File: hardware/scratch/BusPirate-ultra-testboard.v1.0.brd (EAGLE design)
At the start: 40.3 x 44.4 mm, 20 parts, among them J1 CON_HEADER_1X10-RIGHT_ANGLED_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

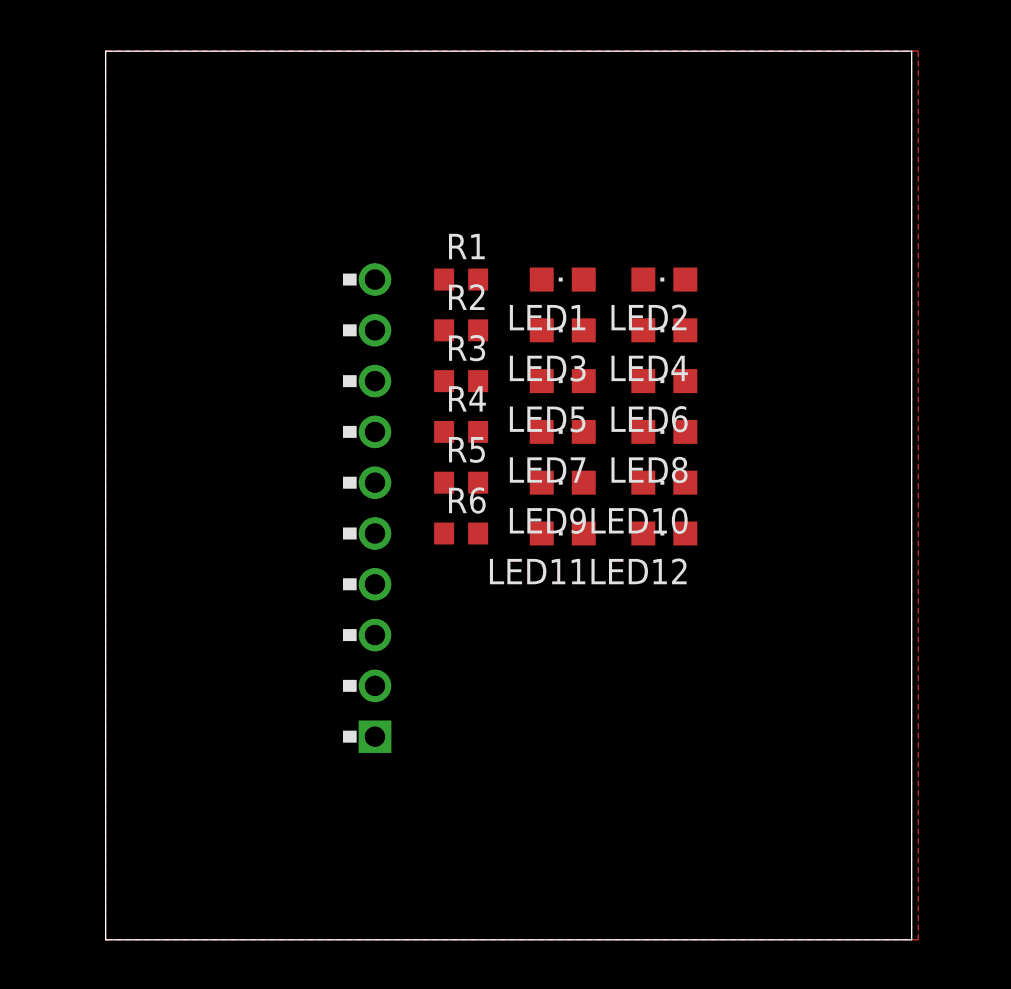
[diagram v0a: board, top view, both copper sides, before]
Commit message: updated BP test board board, added LEDs for 5V and 3.3V
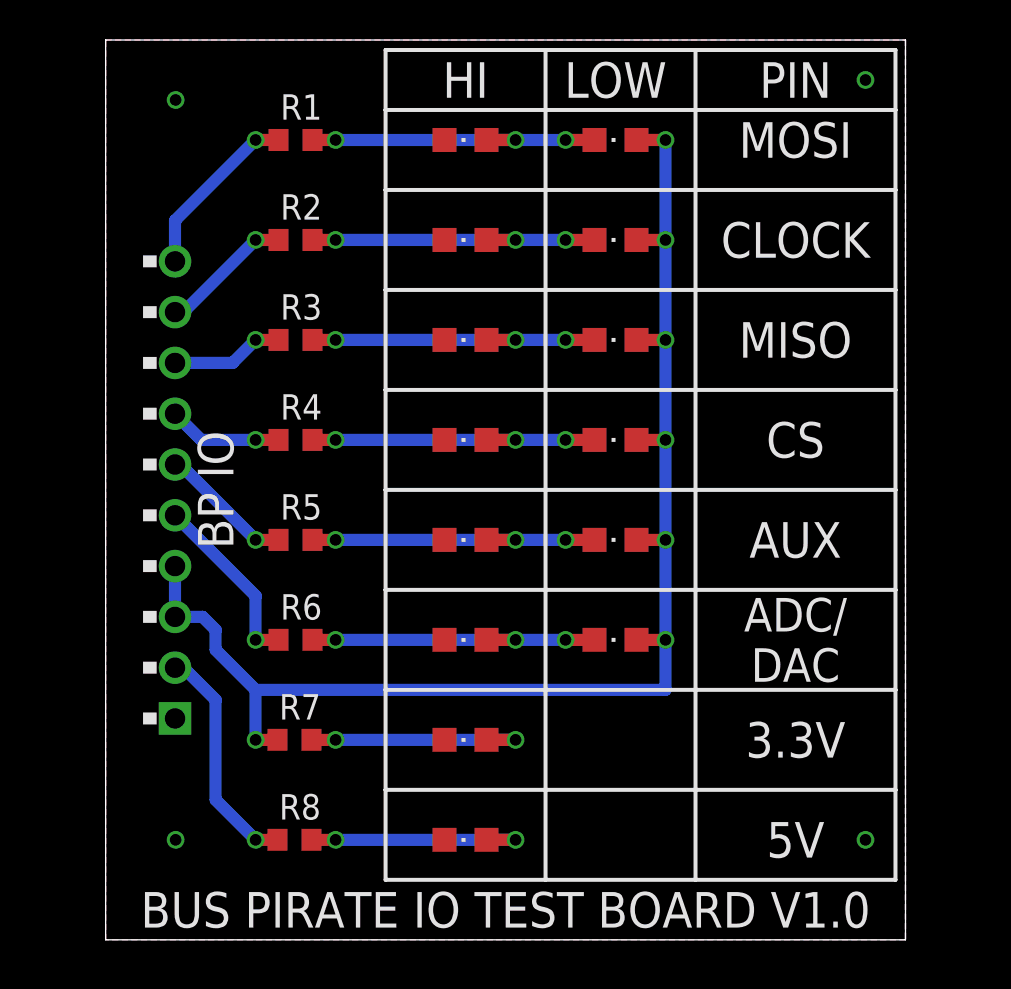
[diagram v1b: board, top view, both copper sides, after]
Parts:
- added LED13, LED14: (no value), dp_devices.v6:LED-805
- added R7, R8: 1k1, dp_devices.v6:R603
- moved R1 10.8 mm to (9.50, 40.0)
- moved J1 10.0 mm to (-2.38, 22.5)
- moved R6 9.84 mm to (9.50, 15.0)
- moved R2 9.43 mm to (9.50, 35.0)
- moved R5 8.76 mm to (9.50, 20.0)
- moved R3 8.53 mm to (9.50, 30.0)
- moved LED1 8.51 mm to (18.0, 40.0)
- moved R4 8.29 mm to (9.50, 25.0)
- moved LED2 7.39 mm to (25.5, 40.0)
- moved LED11 7.21 mm to (18.0, 15.0)
- moved LED3 6.64 mm to (18.0, 35.0)
- moved LED12 5.85 mm to (25.5, 15.0)
- moved LED9 5.64 mm to (18.0, 20.0)
- moved LED5 5.28 mm to (18.0, 30.0)
- moved LED4 5.14 mm to (25.5, 35.0)
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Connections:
- new net 5V0: J1.2, R8.1
- new net N$7: LED14.A, R8.2
- new net N$8: LED13.A, R7.2
- net 3V3: now also J1.4, R7.1
- net GND: now also LED13.C, LED14.C
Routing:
- net 3V3: track 0.00 -> 69.0 mm, vias 0 -> 7
- net N$6: track 0.00 -> 15.5 mm, vias 0 -> 3
- net N$5: track 0.00 -> 15.5 mm, vias 0 -> 3
- net N$4: track 0.00 -> 15.5 mm, vias 0 -> 3
- net N$3: track 0.00 -> 15.5 mm, vias 0 -> 3
- net N$2: track 0.00 -> 15.5 mm, vias 0 -> 3
- net N$1: track 0.00 -> 15.5 mm, vias 0 -> 3
- net N$8: track 0.00 -> 11.7 mm, vias 0 -> 2
- net N$7: track 0.00 -> 11.7 mm, vias 0 -> 2
- net 5V0: track 0.00 -> 11.6 mm, vias 0 -> 1
- net ADC_DAC: track 0.00 -> 9.05 mm, vias 0 -> 1
- net MOSI: track 0.00 -> 8.89 mm, vias 0 -> 1
- net AUX: track 0.00 -> 6.74 mm, vias 0 -> 1
- net CLOCK: track 0.00 -> 6.68 mm, vias 0 -> 1
- net CS: track 0.00 -> 5.72 mm, vias 0 -> 1
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- added copper zone on layer 16, net GND
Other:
- board size 40.3 x 44.4 mm -> 40 x 45 mm
- board text added: "3.3V"
- board text added: "5V"
- board text added: "ADC/ DAC"
- board text added: "AUX"
- board text added: "BP IO"
- board text added: "BUS PIRATE IO TEST BOARD V1.0"
- board text added: "CLOCK"
- board text added: "CS"
- board text added: "Dangerous Prototypes"
- board text added: "HI"
- board text added: "LOW"
- board text added: "MAY 2019"
- board text added: "MISO"
- board text added: "MOSI"
- board text added: "PIN"

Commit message: flipped IO connector
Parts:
- moved LED1 35.0 mm to (18.0, 5.00)
- moved LED14 35.0 mm to (18.0, 40.0)
- moved LED2 35.0 mm to (25.5, 5.00)
- moved R1 35.0 mm to (9.50, 5.00)
- moved R8 35.0 mm to (9.44, 40.0)
- moved LED13 25.0 mm to (18.0, 35.0)
- moved LED3 25.0 mm to (18.0, 10.0)
- moved LED4 25.0 mm to (25.5, 10.0)
- moved R2 25.0 mm to (9.50, 10.0)
- moved R7 25.0 mm to (9.44, 35.0)
- moved LED11 15.0 mm to (18.0, 30.0)
- moved LED12 15.0 mm to (25.5, 30.0)
- moved LED5 15.0 mm to (18.0, 15.0)
- moved LED6 15.0 mm to (25.5, 15.0)
- moved R3 15.0 mm to (9.50, 15.0)
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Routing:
- net 3V3: track 69.0 -> 74.4 mm
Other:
- board text added: "1"
